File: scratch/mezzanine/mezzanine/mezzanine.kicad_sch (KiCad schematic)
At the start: 6 parts, among them J101 Conn_02x35_Counter_Clockwise_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, J102 Conn_2Rows-76Pins

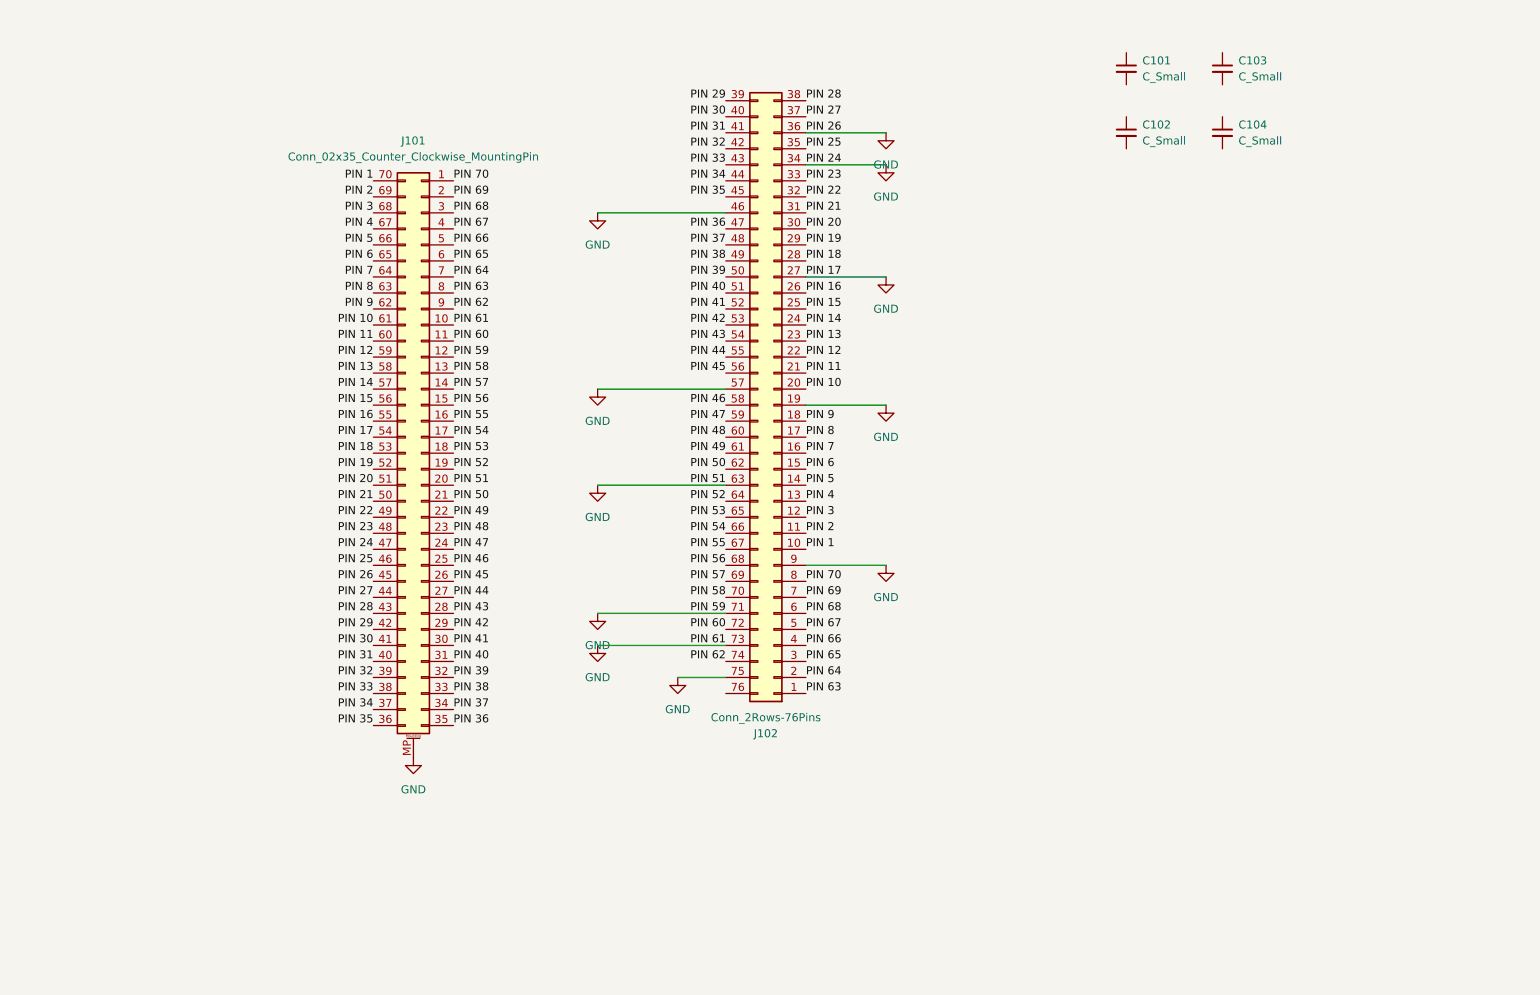
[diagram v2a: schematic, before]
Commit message: create more pretty symbols for mezzanine and padring
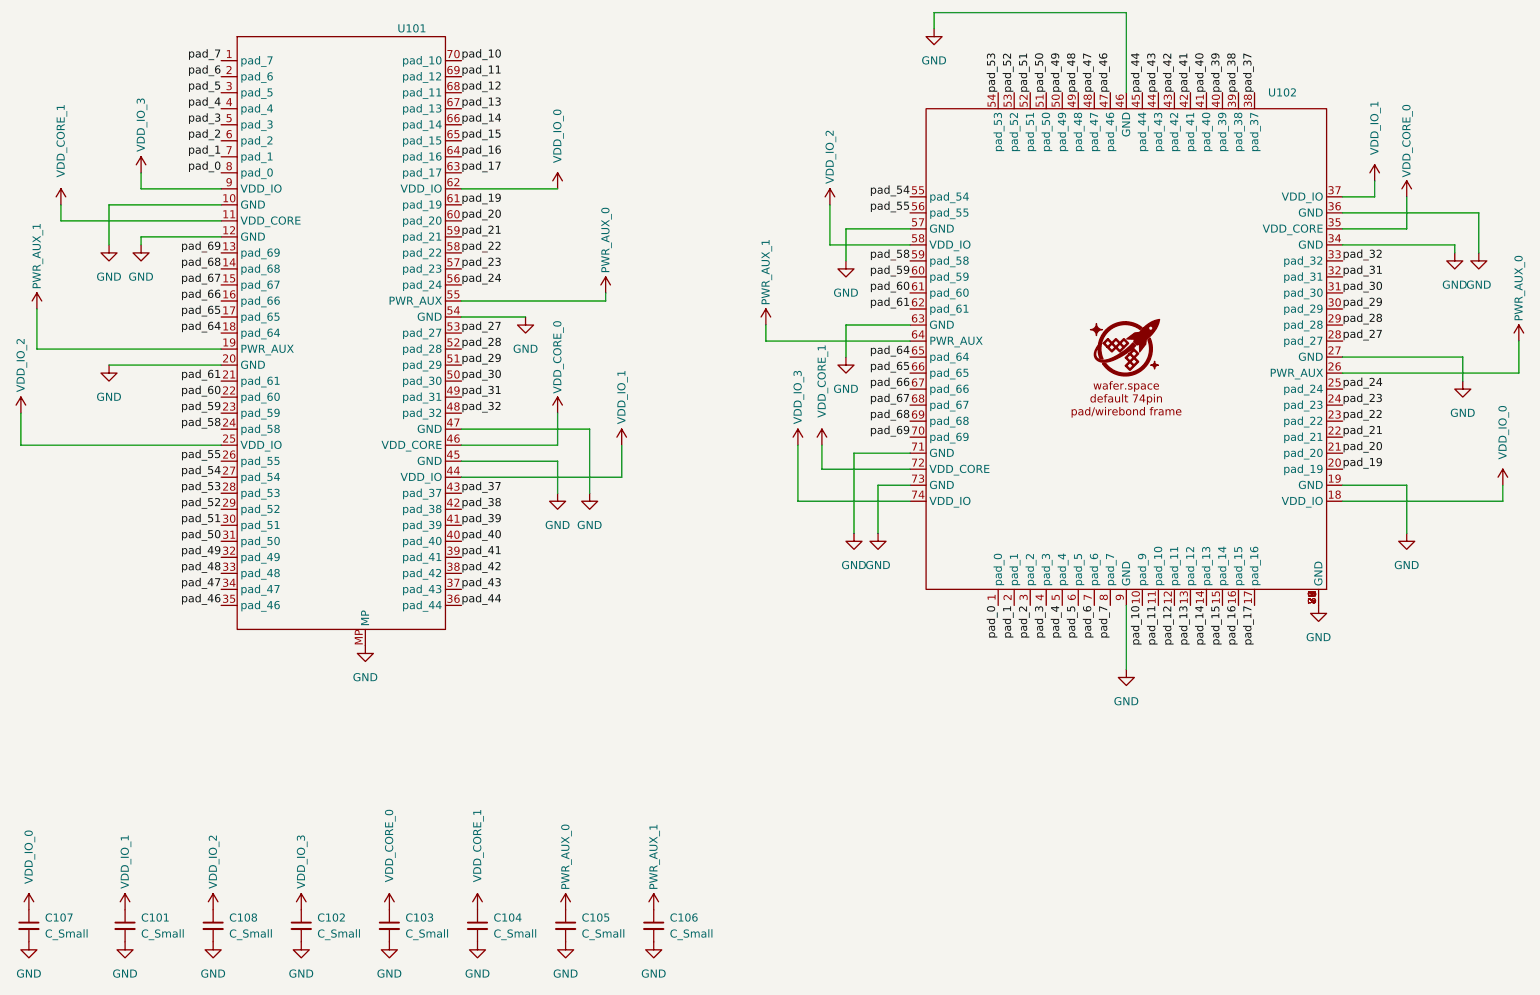
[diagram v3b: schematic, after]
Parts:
- removed J101: Conn_02x35_Counter_Clockwise_MountingPin, Connector_Mezzanine:CONN-SMD_70P-P0.40_HCTL_HC-PBB40C-70DP-0.4V-02, symbol Connector_Generic_MountingPin:Conn_02x35_Counter_Clockwise_MountingPin
- removed J102: Conn_2Rows-76Pins, WafeSpace:waferspace_default_padring_v0.2, symbol Connector_Generic:Conn_02x38_Counter_Clockwise
- added C105, C106, C107, C108: C_Small, Capacitor_SMD:C_0201_0603Metric, symbol Device:C_Small
- added U101: ~, Connector_Mezzanine:CONN-SMD_70P-P0.40_HCTL_HC-PBB40C-70DP-0.4V-02, symbol WaferSpace:70pin_ws_default_mezzanine
- added U102: ~, WafeSpace:waferspace_default_padring_v0.2, symbol WaferSpace:WS_default_74padring
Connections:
- net GND: now also C101.2, C102.2, C103.2, C104.2, C105.2, C106.2, C107.2, C108.2, U101.10 (GND), U101.12 (GND), U101.20 (GND), U101.45 (GND), U101.47 (GND), U101.54 (GND), U101.MP, U102.19 (GND), U102.27 (GND), U102.34 (GND), U102.36 (GND), U102.46 (GND), U102.57 (GND), U102.63 (GND), U102.71 (GND), U102.73 (GND), U102.75 (GND), U102.76 (GND), U102.77 (GND), U102.78 (GND), U102.79 (GND), U102.80 (GND), U102.81 (GND), U102.9 (GND)
- net VDD_IO_1: now reaches C101.1
- net VDD_IO_1: now also U101.44 (VDD_IO), U102.37 (VDD_IO)
- net VDD_CORE_0: now reaches C103.1
- net VDD_CORE_0: now also U101.46 (VDD_CORE), U102.35 (VDD_CORE)
- net VDD_CORE_1: now reaches C104.1
- net VDD_CORE_1: now also U101.11 (VDD_CORE), U102.72 (VDD_CORE)
- net VDD_IO_3: now reaches C102.1
- net VDD_IO_3: now also U101.9 (VDD_IO), U102.74 (VDD_IO)
- new net PWR_AUX_0: C105.1, U101.55 (PWR_AUX), U102.26 (PWR_AUX)
- new net PWR_AUX_1: C106.1, U101.19 (PWR_AUX), U102.64 (PWR_AUX)
- new net VDD_IO_0: C107.1, U101.62 (VDD_IO), U102.18 (VDD_IO)
- new net VDD_IO_2: C108.1, U101.25 (VDD_IO), U102.58 (VDD_IO)
- new net pad_0: U101.8 (pad_0), U102.1 (pad_0)
- new net pad_1: U101.7 (pad_1), U102.2 (pad_1)
- new net pad_10: U101.70 (pad_10), U102.10 (pad_9)
- new net pad_11: U101.69 (pad_12), U102.11 (pad_10)
- new net pad_12: U101.68 (pad_11), U102.12 (pad_11)
- new net pad_13: U101.67 (pad_13), U102.13 (pad_12)
- new net pad_14: U101.66 (pad_14), U102.14 (pad_13)
- new net pad_15: U101.65 (pad_15), U102.15 (pad_14)
- new net pad_16: U101.64 (pad_16), U102.16 (pad_15)
- new net pad_17: U101.63 (pad_17), U102.17 (pad_16)
- new net pad_19: U101.61 (pad_19), U102.20 (pad_19)
- new net pad_2: U101.6 (pad_2), U102.3 (pad_2)
- new net pad_20: U101.60 (pad_20), U102.21 (pad_20)
- new net pad_21: U101.59 (pad_21), U102.22 (pad_21)
- new net pad_22: U101.58 (pad_22), U102.23 (pad_22)
- new net pad_23: U101.57 (pad_23), U102.24 (pad_23)
- new net pad_24: U101.56 (pad_24), U102.25 (pad_24)
- new net pad_27: U101.53 (pad_27), U102.28 (pad_27)
- new net pad_28: U101.52 (pad_28), U102.29 (pad_28)
- new net pad_29: U101.51 (pad_29), U102.30 (pad_29)
- new net pad_3: U101.5 (pad_3), U102.4 (pad_3)
- new net pad_30: U101.50 (pad_30), U102.31 (pad_30)
- new net pad_31: U101.49 (pad_31), U102.32 (pad_31)
- new net pad_32: U101.48 (pad_32), U102.33 (pad_32)
- new net pad_37: U101.43 (pad_37), U102.38 (pad_37)
- new net pad_38: U101.42 (pad_38), U102.39 (pad_38)
- new net pad_39: U101.41 (pad_39), U102.40 (pad_39)
- new net pad_4: U101.4 (pad_4), U102.5 (pad_4)
- new net pad_40: U101.40 (pad_40), U102.41 (pad_40)
- new net pad_41: U101.39 (pad_41), U102.42 (pad_41)
- new net pad_42: U101.38 (pad_42), U102.43 (pad_42)
- new net pad_43: U101.37 (pad_43), U102.44 (pad_43)
- new net pad_44: U101.36 (pad_44), U102.45 (pad_44)
- new net pad_46: U101.35 (pad_46), U102.47 (pad_46)
- new net pad_47: U101.34 (pad_47), U102.48 (pad_47)
- new net pad_48: U101.33 (pad_48), U102.49 (pad_48)
- new net pad_49: U101.32 (pad_49), U102.50 (pad_49)
- new net pad_5: U101.3 (pad_5), U102.6 (pad_5)
- new net pad_50: U101.31 (pad_50), U102.51 (pad_50)
- new net pad_51: U101.30 (pad_51), U102.52 (pad_51)
- new net pad_52: U101.29 (pad_52), U102.53 (pad_52)
- new net pad_53: U101.28 (pad_53), U102.54 (pad_53)
- new net pad_54: U101.27 (pad_54), U102.55 (pad_54)
- new net pad_55: U101.26 (pad_55), U102.56 (pad_55)
- new net pad_58: U101.24 (pad_58), U102.59 (pad_58)
- new net pad_59: U101.23 (pad_59), U102.60 (pad_59)
- new net pad_6: U101.2 (pad_6), U102.7 (pad_6)
- new net pad_60: U101.22 (pad_60), U102.61 (pad_60)
- new net pad_61: U101.21 (pad_61), U102.62 (pad_61)
- new net pad_64: U101.18 (pad_64), U102.65 (pad_64)
- new net pad_65: U101.17 (pad_65), U102.66 (pad_65)
- new net pad_66: U101.16 (pad_66), U102.67 (pad_66)
- new net pad_67: U101.15 (pad_67), U102.68 (pad_67)
- new net pad_68: U101.14 (pad_68), U102.69 (pad_68)
- new net pad_69: U101.13 (pad_69), U102.70 (pad_69)
- new net pad_7: U101.1 (pad_7), U102.8 (pad_7)
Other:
- moved on the sheet: C101

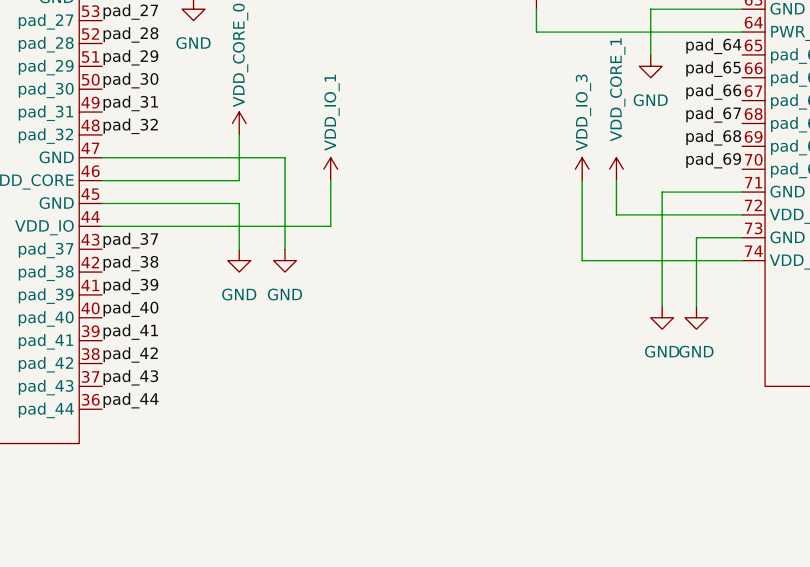
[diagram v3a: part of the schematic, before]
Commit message: broken wires
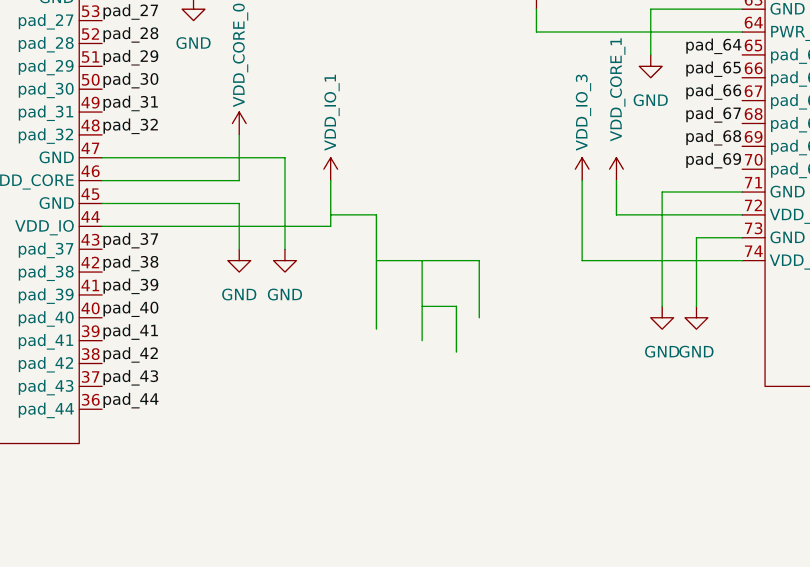
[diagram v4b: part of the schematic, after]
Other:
- company: (none) -> Evezor Inc
- title: (none) -> wafer.space default digital chip-on-board mezzanine
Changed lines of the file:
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@@
 	(generator_version "9.0")
 	(paper "A4")
+	(title_block
+		(title "wafer.space default digital chip-on-board mezzanine")
+		(date "2025-10-23")
+		(rev "0")
+		(company "Evezor Inc")
+	)
 	(wire
 		(pts
@@
 	(wire
 		(pts
+			(xy 138.43 123.19) (xy 138.43 114.3)
+		)
+		(stroke
+			(width 0)
+			(type default)
+		)
+	)
+	(wire
+		(pts
 			(xy 242.57 66.04) (xy 247.65 66.04)
 		)
@@
 	(wire
 		(pts
+			(xy 144.78 120.65) (xy 144.78 114.3)
+		)
+		(stroke
+			(width 0)
+			(type default)
+		)
+	)
+	(wire
+		(pts
 			(xy 102.87 105.41) (xy 118.11 105.41)
 		)
@@
 	(wire
 		(pts
+			(xy 133.35 114.3) (xy 144.78 114.3)
+		)
+		(stroke
+			(width 0)
+			(type default)
+		)
+	)
+	(wire
+		(pts
 			(xy 64.77 72.39) (xy 52.07 72.39)
 		)
@@
 	(wire
 		(pts
+			(xy 133.35 109.22) (xy 128.27 109.22)
+		)
+		(stroke
+			(width 0)
+			(type default)
+		)
+	)
+	(wire
+		(pts
 			(xy 242.57 71.12) (xy 252.73 71.12)
 		)
@@
 	(wire
 		(pts
+			(xy 133.35 121.92) (xy 133.35 109.22)
+		)
+		(stroke
+			(width 0)
+			(type default)
+		)
+	)
+	(wire
+		(pts
 			(xy 64.77 67.31) (xy 46.99 67.31)
 		)
@@
 	(wire
 		(pts
+			(xy 142.24 124.46) (xy 142.24 119.38)
+		)
+		(stroke
+			(width 0)
+			(type default)
+		)
+	)
+	(wire
+		(pts
 			(xy 242.57 114.3) (xy 267.97 114.3)
 		)
@@
 		)
 		(stroke
+			(width 0)
+			(type default)
+		)
+	)
+	(wire
+		(pts
+			(xy 142.24 119.38) (xy 138.43 119.38)
+		)
+		(stroke

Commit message: housekeeping
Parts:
- added U2: ~, WaferSpace:P0.40_HC-PBB40C-70DS-0.4V-3.0-02_wscob, symbol WaferSpace:70pin_ws_default_mezzanine_TT
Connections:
- net pad_17 is gone; now on net pad_16: U101.63 (pad_16), U102.17 (pad_16)
- net GND: now also U101.18 (GND), U101.25 (GND), U101.53 (GND), U101.61 (GND); no longer U101.12 (GND), U101.20 (GND), U101.47 (GND), U101.54 (GND)
- net PWR_AUX_0: now also U101.54 (PWR_AUX); no longer U101.55 (PWR_AUX)
- net VDD_IO_2: now also U101.24 (VDD_IO); no longer U101.25 (VDD_IO)
- net pad_10: now also U101.69 (pad_10), U102.11 (pad_10); no longer U101.70 (pad_10), U102.10 (pad_9)
- net pad_11: now also U101.68 (pad_11), U102.12 (pad_11); no longer U101.69 (pad_12), U102.11 (pad_10)
- net pad_12: now also U101.67 (pad_12), U102.13 (pad_12); no longer U101.68 (pad_11), U102.12 (pad_11)
- net pad_13: now also U101.66 (pad_13), U102.14 (pad_13); no longer U101.67 (pad_13), U102.13 (pad_12)
- net pad_14: now also U101.65 (pad_14), U102.15 (pad_14); no longer U101.66 (pad_14), U102.14 (pad_13)
- net pad_15: now also U101.64 (pad_15), U102.16 (pad_15); no longer U101.65 (pad_15), U102.15 (pad_14)
- net pad_16: no longer U101.64 (pad_16), U102.16 (pad_15)
- net pad_19: now also U101.60 (pad_19); no longer U101.61 (pad_19)
- net pad_20: now also U101.59 (pad_20); no longer U101.60 (pad_20)
- net pad_21: now also U101.58 (pad_21); no longer U101.59 (pad_21)
- net pad_22: now also U101.57 (pad_22); no longer U101.58 (pad_22)
- net pad_23: now also U101.56 (pad_23); no longer U101.57 (pad_23)
- net pad_24: now also U101.55 (pad_24); no longer U101.56 (pad_24)
- net pad_27: now also U101.52 (pad_27); no longer U101.53 (pad_27)
- net pad_28: now also U101.51 (pad_28); no longer U101.52 (pad_28)
- net pad_29: now also U101.50 (pad_29); no longer U101.51 (pad_29)
- net pad_30: now also U101.49 (pad_30); no longer U101.50 (pad_30)
- net pad_31: now also U101.48 (pad_31); no longer U101.49 (pad_31)
- net pad_32: now also U101.47 (pad_32); no longer U101.48 (pad_32)
- net pad_58: now also U101.23 (pad_58); no longer U101.24 (pad_58)
- net pad_59: now also U101.22 (pad_59); no longer U101.23 (pad_59)
- net pad_60: now also U101.21 (pad_60); no longer U101.22 (pad_60)
- net pad_61: now also U101.20 (pad_61); no longer U101.21 (pad_61)
- net pad_64: now also U101.17 (pad_64); no longer U101.18 (pad_64)
- net pad_65: now also U101.16 (pad_65); no longer U101.17 (pad_65)
- net pad_66: now also U101.15 (pad_66); no longer U101.16 (pad_66)
- net pad_67: now also U101.14 (pad_67); no longer U101.15 (pad_67)
- net pad_68: now also U101.13 (pad_68); no longer U101.14 (pad_68)
- net pad_69: now also U101.12 (pad_69); no longer U101.13 (pad_69)
- new net: U2.10 (GND), U2.18 (GND), U2.25 (GND), U2.45 (GND), U2.53 (GND), U2.61 (GND), U2.MP (GND)
- new net pad_9: U101.70 (pad_9), U102.10 (pad_9)
